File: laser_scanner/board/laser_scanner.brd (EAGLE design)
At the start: 22.9 x 38.1 mm, 8 parts

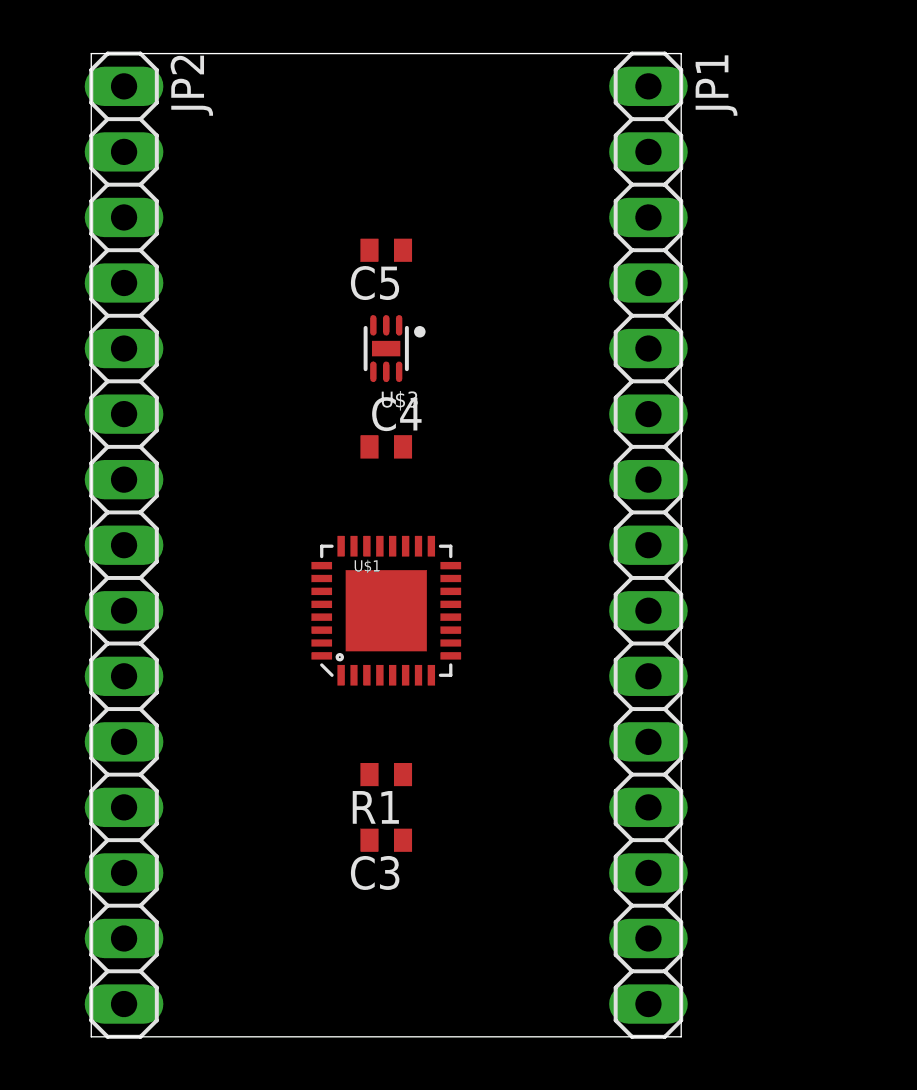
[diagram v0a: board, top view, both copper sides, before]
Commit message: First pass at Othermilled laser scanner board. About to update for Bay Area Circuits order.
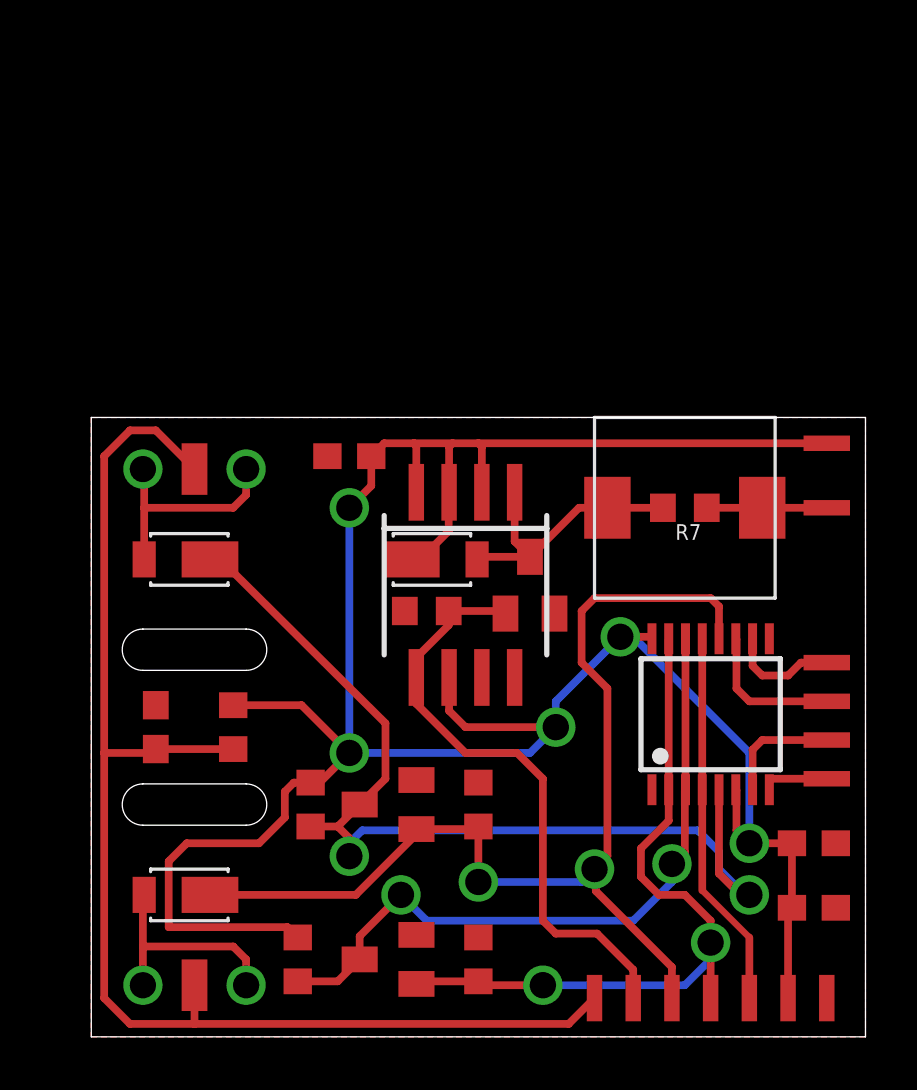
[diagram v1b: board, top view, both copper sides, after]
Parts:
- removed C5: 2.2uF, rcl:C0402
- removed JP1, JP2: (no value), pinhead:1X15
- added C1: 100nF, rcl:C0603
- added C2: 1uF, rcl:C0603
- added GALVO_DIR, GALVO_PULSE, GALVO_SEL, GALVO_SENSE, GND, L+, L-, LASER_PWM, MA1, MA2, MB1, MB2, VCC: PAD-0.6_1.8, modular_robotics:PAD_0.6_1.8
- added L1: 1mH, modular_robotics:L7070
- added Q1, Q2, Q3: BSS123, transistor-small-signal:SOT23
- added R2, R3, R4, R5, R6: 10k, rcl:R0603
- added R7: 50R, rcl:R0603
- added U$14, U$2, U$6: DFLS130L, modular_robotics:POWERDI123
- added U$7: LASER_SLIDER, modular_robotics:LASER_SCANNER
- C3: value 0.1uF -> 100nF; device rcl:C0402 -> rcl:C0603
- C4: value 2.2uF -> 1uF; device rcl:C0402 -> rcl:C0603
- R1: device rcl:R0402 -> rcl:R0603
- U$1: value STM32L432KCU6 -> TB6552; device modular_robotics:QFN-32 -> modular_robotics:TSSOP16
- U$3: value MIC5305-MLF -> BD6211; device modular_robotics:MLF-6 -> modular_robotics:SOP-08
- moved U$1 13.2 mm to (24.0, 12.5)
- moved C3 9.95 mm to (2.50, 12.0), turned to 90 degrees
- moved U$3 9.67 mm to (14.5, 17.5)
- moved R1 7.94 mm to (8.00, 3.00), turned to 90 degrees
- moved C4 1.47 mm to (10.0, 22.5), turned to 180 degrees
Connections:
- removed net +5V: JP1.4
- removed net NRST: JP1.3, JP2.3, U$1.4
- removed net PA0: JP1.12, U$1.6
- removed net PA1: JP1.11, U$1.7
- removed net PA10: JP2.2, U$1.20
- removed net PA11: JP2.13, U$1.21
- removed net PA12: JP2.5, U$1.22
- removed net PA13: U$1.23
- removed net PA14: U$1.24
- removed net PA15: U$1.25
- removed net PA2: JP1.5, U$1.8
- removed net PA3: JP1.10, U$1.9
- removed net PA4: JP1.9, U$1.10
- removed net PA5: JP1.8, U$1.11
- removed net PA6: JP1.7, U$1.12
- removed net PA7: JP1.6, U$1.13
- removed net PA8: JP2.12, U$1.18
- removed net PA9: JP2.1, U$1.19
- removed net PB0: JP2.6, U$1.14
- removed net PB1: JP2.9, U$1.15
- removed net PB3: JP1.15, U$1.26
- removed net PB4: JP2.15, U$1.27
- removed net PB5: JP2.14, U$1.28
- removed net PB6: JP2.8, U$1.29
- removed net PB7: JP2.7, U$1.30
- removed net PF0: JP2.10, U$1.2
- removed net PF1: JP2.11, U$1.3
- removed net VCC: C5.1, JP1.1, U$3.1, U$3.3
- new net N$10: LASER_PWM.1, Q3.1, R6.2, U$3.5
- new net N$11: U$14.A, U$7.A1, U$7.A3
- new net N$12: L1.1, Q3.3, R7.2, U$2.A, U$3.1
- new net N$13: U$6.A, U$7.B1, U$7.B3
- new net N$14: C3.1, GALVO_SENSE.1, R2.1, U$7.A2, U$7.B2
- new net N$15: L-.1, L1.2, R7.1
- new net N$17: Q2.3, R5.1, U$1.5, U$14.C
- new net N$2: MB2.1, U$1.8
- new net N$3: MA1.1, U$1.11
- new net N$4: MA2.1, U$1.10
- new net N$5: Q1.3, R1.1, U$1.14, U$1.3
- new net N$6: GALVO_SEL.1, Q2.1, R4.2, U$1.12, U$6.C
- new net N$7: GALVO_DIR.1, Q1.1, R3.2, U$1.15, U$1.2
- new net N$9: GALVO_PULSE.1, U$1.13, U$1.4
- net +3V3: now also C1.1, C2.1, L+.1, R1.2, R2.2, R5.2, U$1.16, U$1.6, U$2.C, U$3.2, U$3.3, U$3.6, VCC.1; no longer C3.1, JP1.13, JP1.14, U$1.1, U$1.17, U$1.5
- net GND: now also C1.2, C2.2, GND.1, Q1.2, Q2.2, Q3.2, R3.1, R4.1, R6.1, U$1.1, U$1.9, U$3.8; no longer C5.2, JP1.2, JP2.4, R1.1, U$1.16, U$1.32, U$3.2
- net N$1: now also MB1.1, U$1.7; no longer R1.2, U$1.31
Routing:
- net +3V3: track 0.00 -> 101.5 mm, vias 0 -> 5
- net N$14: track 0.00 -> 51.9 mm
- net N$6: track 0.00 -> 42.3 mm, vias 0 -> 2
- net N$17: track 0.00 -> 39.0 mm, vias 0 -> 2
- net N$7: track 0.00 -> 28.6 mm, vias 0 -> 2
- net N$5: track 0.00 -> 27.1 mm, vias 0 -> 2
- net N$10: track 0.00 -> 23.4 mm
- net N$9: track 0.00 -> 14.7 mm
- net N$12: track 0.00 -> 10.8 mm
- net N$13: track 0.00 -> 8.73 mm
- net N$11: track 0.00 -> 8.68 mm
- net N$3: track 0.00 -> 5.64 mm
- net N$15: track 0.00 -> 4.65 mm
- net N$1: track 0.00 -> 4.58 mm
- net N$4: track 0.00 -> 4.29 mm
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- added copper zone on layer 1, net GND
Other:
- board size 22.9 x 38.1 mm -> 30 x 24 mm

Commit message: Reworked laser scanner for BAC order
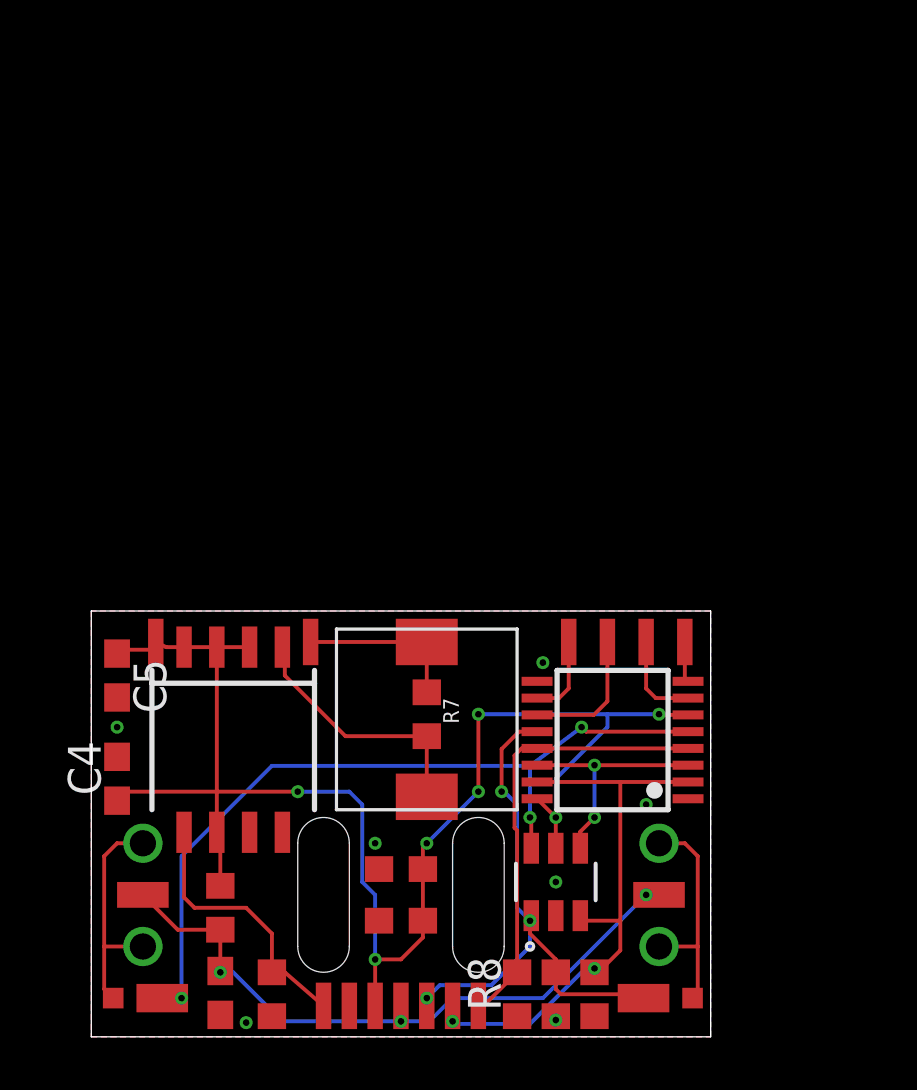
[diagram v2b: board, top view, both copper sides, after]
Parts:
- removed Q1, Q2, Q3: BSS123, transistor-small-signal:SOT23
- removed R1, R5: 10k, rcl:R0603
- added C5: 100nF, rcl:C0603
- added R8: 10k, rcl:R0603
- U$14, U$6: device modular_robotics:POWERDI123 -> modular_robotics:POWERDI323
- U$2: value DFLS130L -> 742G14; device modular_robotics:POWERDI123 -> modular_robotics:SOT23-6
- moved L+ 27.1 mm to (2.50, 15.3), turned to 0 degrees
- moved L- 20.7 mm to (8.50, 15.3), turned to 180 degrees
- moved U$6 19.6 mm to (22.1, 1.50), turned to 0 degrees
- moved GND 18.5 mm to (10.0, 1.20), turned to 180 degrees
- moved U$14 17.0 mm to (2.00, 1.50)
- moved C2 16.3 mm to (12.0, 4.50), turned to 180 degrees
- moved C1 16.1 mm to (12.0, 6.50), turned to 180 degrees
- moved R6 16.0 mm to (7.00, 1.65), turned to 90 degrees
- moved VCC 16.0 mm to (11.0, 1.20), turned to 180 degrees
- moved C4 15.4 mm to (1.00, 10.0), turned to 90 degrees
- moved U$2 13.1 mm to (18.0, 6.00)
- moved L1 12.9 mm to (13.0, 12.3), turned to 180 degrees
- moved R7 12.8 mm to (13.0, 12.5), turned to 270 degrees
- moved LASER_PWM 12.0 mm to (9.00, 1.20), turned to 180 degrees
- moved U$3 10.8 mm to (5.50, 11.5)
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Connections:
- net +3V3: now also C5.1, U$2.5; no longer R1.2, R5.2, U$2.C
- net GND: now also C5.2, R8.1, U$2.2; no longer Q1.2, Q2.2, Q3.2
- net N$10: no longer Q3.1
- net N$12: no longer Q3.3, U$2.A
- net N$17: now also U$2.6; no longer Q2.3, R5.1
- net N$5: now also U$2.4; no longer Q1.3, R1.1
- net N$6: now also U$2.1; no longer Q2.1
- net N$7: now also U$2.3; no longer Q1.1
- net N$9: now also R8.2
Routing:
- net +3V3: track 101.5 -> 59.6 mm, vias 5 -> 7
- net N$14: track 51.9 -> 25.7 mm, vias 0 -> 3
- net N$6: track 42.3 -> 21.8 mm, vias 2 -> 3
- net N$5: track 27.1 -> 9.30 mm
- net N$10: track 23.4 -> 10.5 mm
- net N$17: track 39.0 -> 31.1 mm, vias 2 -> 3
- net N$7: track 28.6 -> 22.4 mm
- net N$9: track 14.7 -> 17.3 mm
- net N$15: track 4.65 -> 6.45 mm
- net N$4: track 4.29 -> 3.18 mm
- net N$2: track 2.65 -> 1.58 mm
- net N$1: track 4.58 -> 3.58 mm
- net N$12: track 10.8 -> 9.96 mm
- added copper zone on layer 16, net GND
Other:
- board size 30 x 24 mm -> 24 x 16.5 mm

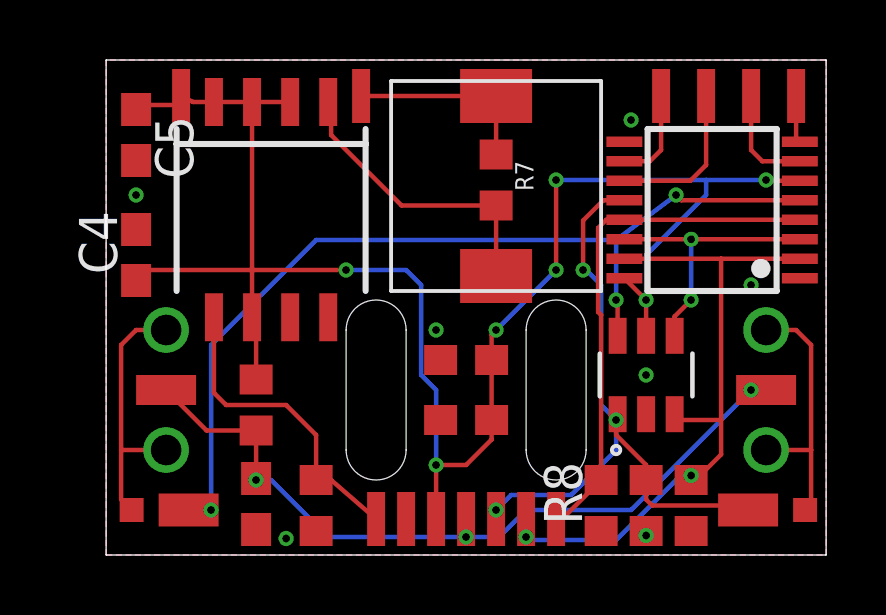
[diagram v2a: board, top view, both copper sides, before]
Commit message: Adding panelized laser scanner board.
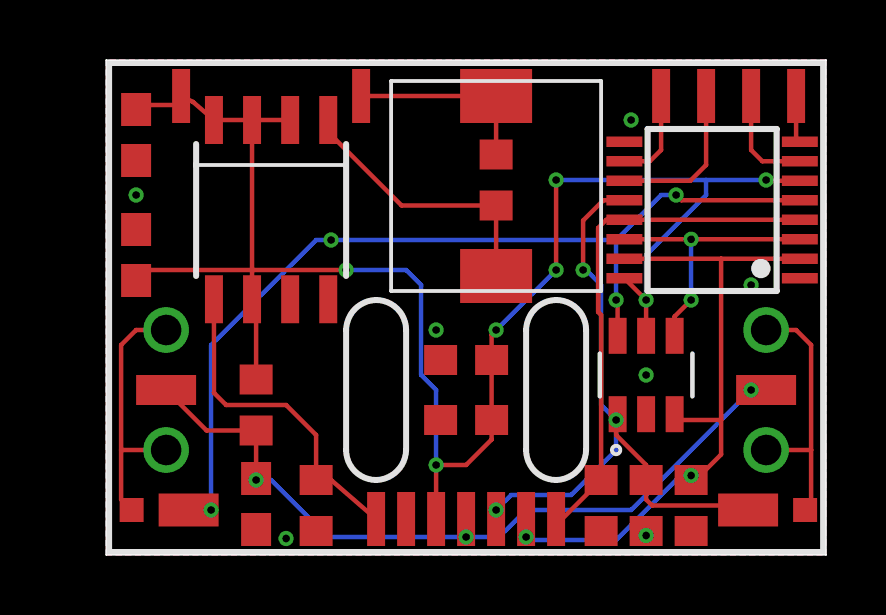
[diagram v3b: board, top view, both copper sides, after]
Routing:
- net N$10: track 10.5 -> 11.1 mm

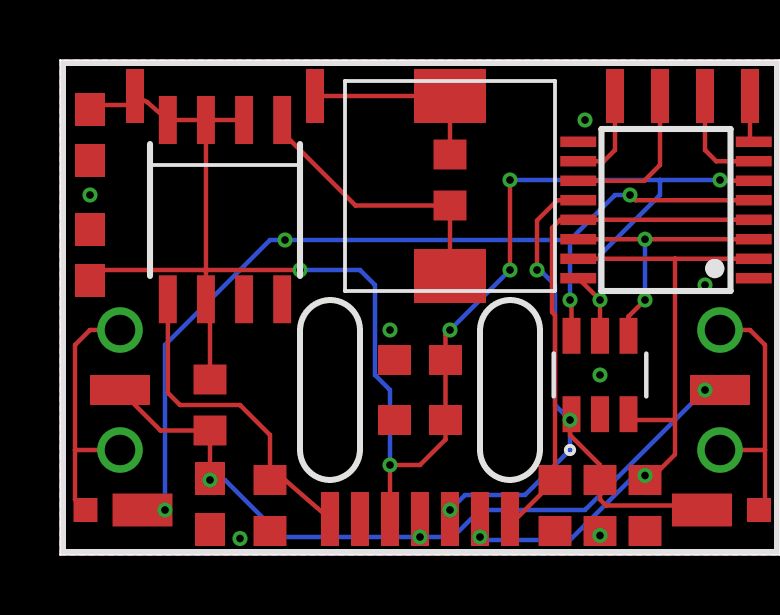
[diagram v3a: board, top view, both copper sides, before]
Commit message: Added labels to wires. Fixed signal running through ground via.
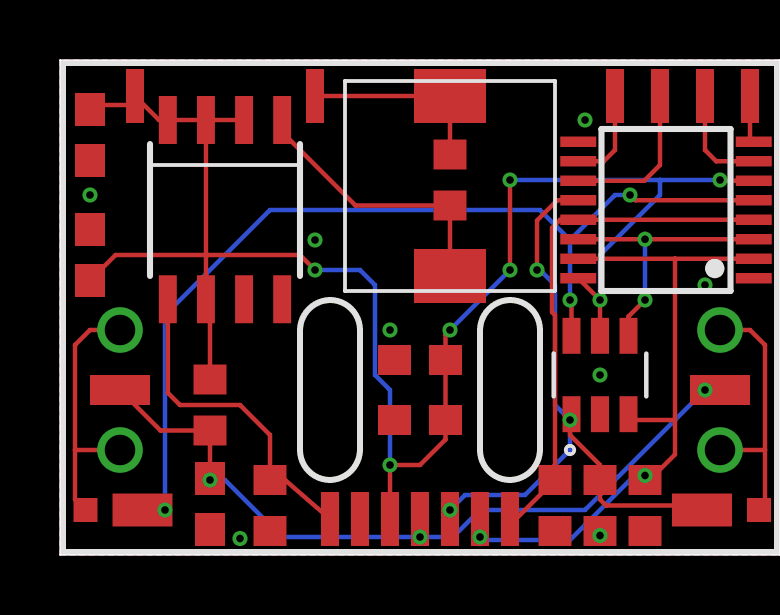
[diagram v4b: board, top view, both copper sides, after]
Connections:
- net N$10 renamed LASER_PWM
- net N$14 renamed SENSE
- net N$6 renamed SEL
- net N$7 renamed DIR
- net N$9 renamed PULSE
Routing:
- net N$17: track 31.2 -> 32.6 mm
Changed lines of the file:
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@@
 <layer number="20" name="Dimension" color="15" fill="1" visible="yes" active="yes"/>
 <layer number="21" name="tPlace" color="7" fill="1" visible="yes" active="yes"/>
-<layer number="22" name="bPlace" color="7" fill="1" visible="no" active="yes"/>
+<layer number="22" name="bPlace" color="7" fill="1" visible="yes" active="yes"/>
 <layer number="23" name="tOrigins" color="15" fill="1" visible="yes" active="yes"/>
-<layer number="24" name="bOrigins" color="15" fill="1" visible="no" active="yes"/>
-<layer number="25" name="tNames" color="7" fill="1" visible="yes" active="yes"/>
+<layer number="24" name="bOrigins" color="15" fill="1" visible="yes" active="yes"/>
+<layer number="25" name="tNames" color="7" fill="1" visible="no" active="yes"/>
 <layer number="26" name="bNames" color="7" fill="1" visible="no" active="yes"/>
-<layer number="27" name="tValues" color="7" fill="1" visible="yes" active="yes"/>
+<layer number="27" name="tValues" color="7" fill="1" visible="no" active="yes"/>
 <layer number="28" name="bValues" color="7" fill="1" visible="no" active="yes"/>
-<layer number="29" name="tStop" color="7" fill="3" visible="yes" active="yes"/>
+<layer number="29" name="tStop" color="7" fill="3" visible="no" active="yes"/>
 <layer number="30" name="bStop" color="7" fill="6" visible="no" active="yes"/>
 <layer number="31" name="tCream" color="7" fill="4" visible="no" active="yes"/>
@@
 <layer number="49" name="Reference" color="7" fill="1" visible="no" active="yes"/>
 <layer number="50" name="dxf" color="7" fill="1" visible="no" active="no"/>
-<layer number="51" name="tDocu" color="7" fill="1" visible="no" active="yes"/>
-<layer number="52" name="bDocu" color="7" fill="1" visible="no" active="yes"/>
+<layer number="51" name="tDocu" color="7" fill="1" visible="yes" active="yes"/>
+<layer number="52" name="bDocu" color="7" fill="1" visible="yes" active="yes"/>
 <layer number="53" name="tGND_GNDA" color="7" fill="9" visible="no" active="no"/>
 <layer number="54" name="bGND_GNDA" color="1" fill="9" visible="no" active="no"/>
@@
 <contactref element="C5" pad="2"/>
 <via x="1" y="12" extent="1-16" drill="0.254"/>
-<via x="7.5" y="10.5" extent="1-16" drill="0.254"/>
+<via x="8.5" y="10.5" extent="1-16" drill="0.254"/>
 </signal>
 <signal name="+3V3">
@@
 <wire x1="4.865" y1="8.525" x2="5" y2="7.79" width="0.15" layer="1"/>
 <wire x1="5" y1="7.79" x2="5" y2="5.85" width="0.15" layer="1"/>
-<wire x1="4.865" y1="8.525" x2="4.865" y2="9.5" width="0.15" layer="1"/>
-<wire x1="4.865" y1="9.5" x2="4.865" y2="14.5" width="0.15" layer="1"/>
+<wire x1="4.865" y1="8.525" x2="4.865" y2="10" width="0.15" layer="1"/>
+<wire x1="4.865" y1="10" x2="4.865" y2="14.5" width="0.15" layer="1"/>
 <wire x1="4.865" y1="14.5" x2="3.595" y2="14.5" width="0.15" layer="1"/>
 <wire x1="4.865" y1="14.5" x2="6.135" y2="14.5" width="0.15" layer="1"/>
@@
 <wire x1="22.025" y1="12.475" x2="22" y2="12.5" width="0.15" layer="1"/>
 <via x="22" y="12.5" extent="1-16" drill="0.254"/>
-<via x="8" y="9.5" extent="1-16" drill="0.254"/>
+<via x="8.5" y="9.5" extent="1-16" drill="0.254"/>
 <wire x1="18" y1="7.306" x2="18" y2="8.5" width="0.15" layer="1"/>
 <via x="18" y="8.5" extent="1-16" drill="0.254"/>
@@
 <wire x1="12.85" y1="3.85" x2="12" y2="3" width="0.15" layer="1"/>
 <wire x1="12" y1="3" x2="11" y2="3" width="0.15" layer="1"/>
-<wire x1="3.595" y1="14.5" x2="2.9" y2="15.1" width="0.15" layer="1"/>
-<wire x1="2.9" y1="15.1" x2="2.5" y2="15.3" width="0.15" layer="1"/>
 <wire x1="2.5" y1="15.3" x2="2.5" y2="15" width="0.15" layer="1"/>
 <wire x1="2.5" y1="15" x2="1.15" y2="15" width="0.15" layer="1"/>
@@
 <wire x1="17.275" y1="9.225" x2="18" y2="8.5" width="0.15" layer="1"/>
 <wire x1="10.5" y1="9" x2="10" y2="9.5" width="0.15" layer="16"/>
-<wire x1="10" y1="9.5" x2="8" y2="9.5" width="0.15" layer="16"/>
-<wire x1="8" y1="9.5" x2="4.865" y2="9.5" width="0.15" layer="1"/>
+<wire x1="10" y1="9.5" x2="8.5" y2="9.5" width="0.15" layer="16"/>
 <wire x1="11" y1="1.2" x2="11" y2="3" width="0.15" layer="1"/>
-<wire x1="4.865" y1="9.5" x2="1.35" y2="9.5" width="0.15" layer="1"/>
-<wire x1="1.35" y1="9.5" x2="1" y2="9.15" width="0.15" layer="1"/>
-</signal>
-<signal name="N$7">
+<wire x1="8.5" y1="9.5" x2="8" y2="10" width="0.15" layer="1"/>
+<wire x1="8" y1="10" x2="4.865" y2="10" width="0.15" layer="1"/>
+<wire x1="4.865" y1="10" x2="1.85" y2="10" width="0.15" layer="1"/>
+<wire x1="1.85" y1="10" x2="1" y2="9.15" width="0.15" layer="1"/>
+<wire x1="3.595" y1="14.5" x2="3.3" y2="14.5" width="0.15" layer="1"/>
+<wire x1="3.3" y1="14.5" x2="2.5" y2="15.3" width="0.15" layer="1"/>
+</signal>
+<signal name="DIR">
 <contactref element="R3" pad="2"/>
 <contactref element="U$1" pad="2"/>
@@
 <wire x1="19.8" y1="2.65" x2="20.5" y2="3.35" width="0.15" layer="1"/>
 </signal>
-<signal name="N$6">
+<signal name="SEL">
 <contactref element="U$6" pad="C"/>
 <contactref element="GALVO_SEL" pad="1"/>
@@
 <wire x1="16" y1="9.5" x2="16.5" y2="9" width="0.15" layer="16"/>
 </signal>
-<signal name="N$9">
+<signal name="PULSE">
 <contactref element="U$1" pad="4"/>
 <contactref element="U$1" pad="13"/>
@@
 <wire x1="23" y1="7.5" x2="22" y2="7.5" width="0.15" layer="1"/>
 </signal>
-<signal name="N$14">
+<signal name="SENSE">
 <contactref element="U$7" pad="A2"/>
 <contactref element="U$7" pad="B2"/>
@@
 <wire x1="13.1" y1="0.6" x2="12" y2="0.6" width="0.15" layer="16"/>
 </signal>
-<signal name="N$10">
+<signal name="LASER_PWM">
 <contactref element="R6" pad="2"/>
 <contactref element="LASER_PWM" pad="1"/>
@@
 <wire x1="2.75" y1="1.5" x2="3.5" y2="1.5" width="0.15" layer="1"/>
 <via x="3.5" y="1.5" extent="1-16" drill="0.254"/>
-<wire x1="3.5" y1="1.5" x2="3.5" y2="7" width="0.15" layer="16"/>
-<wire x1="3.5" y1="7" x2="7" y2="10.5" width="0.15" layer="16"/>
-<wire x1="7" y1="10.5" x2="17" y2="10.5" width="0.15" layer="16"/>
+<wire x1="3.5" y1="1.5" x2="3.5" y2="8" width="0.15" layer="16"/>
 <wire x1="19" y1="12" x2="18.5" y2="12" width="0.15" layer="16"/>
 <wire x1="18.5" y1="12" x2="17" y2="10.5" width="0.15" layer="16"/>
+<wire x1="3.5" y1="8" x2="7" y2="11.5" width="0.15" layer="16"/>
+<wire x1="7" y1="11.5" x2="16" y2="11.5" width="0.15" layer="16"/>
+<wire x1="16" y1="11.5" x2="17" y2="10.5" width="0.15" layer="16"/>
 </signal>
 </signals>
